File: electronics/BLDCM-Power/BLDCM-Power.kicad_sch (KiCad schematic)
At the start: 34 parts, among them J1 501920-3001, J2 53048-0310, J3 505578-0460, J4 505578-0460, J5 FTSH-107-01-L-DV-K, J6 12402012E212A, U1 INA239-Q1, U3 TMC6300-LA, U4 INA239-Q1, U5 TCAN1462, U6 INA239-Q1, U7 BAT54S

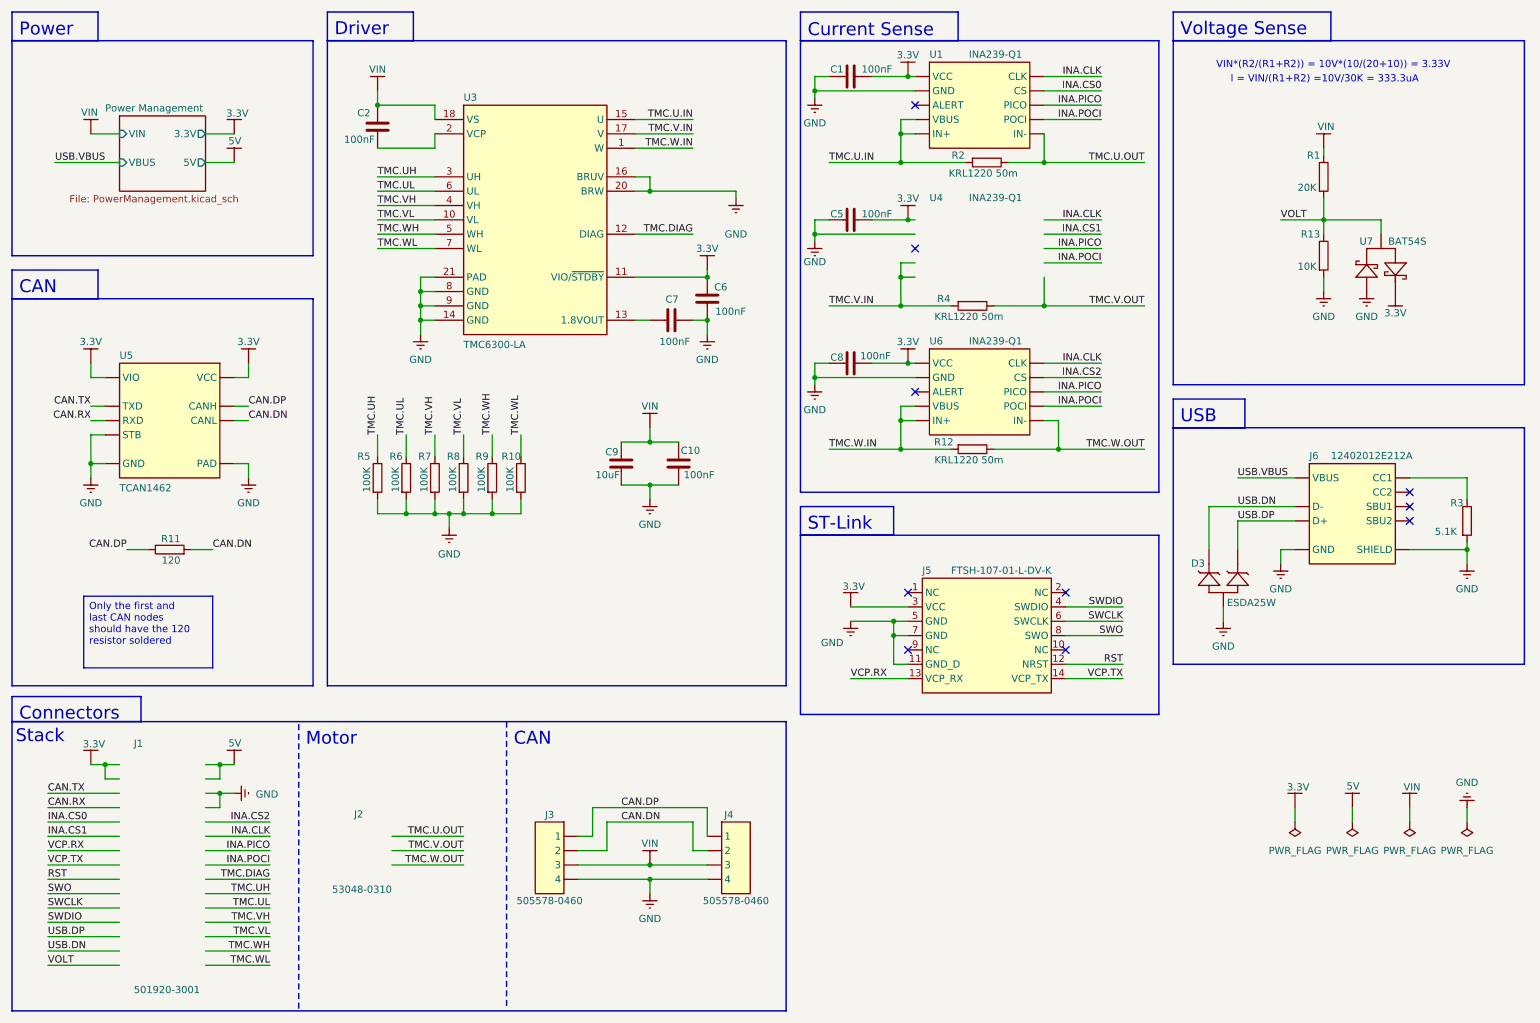
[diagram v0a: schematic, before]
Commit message: Feat(schematic): Replace INA239 with INA240
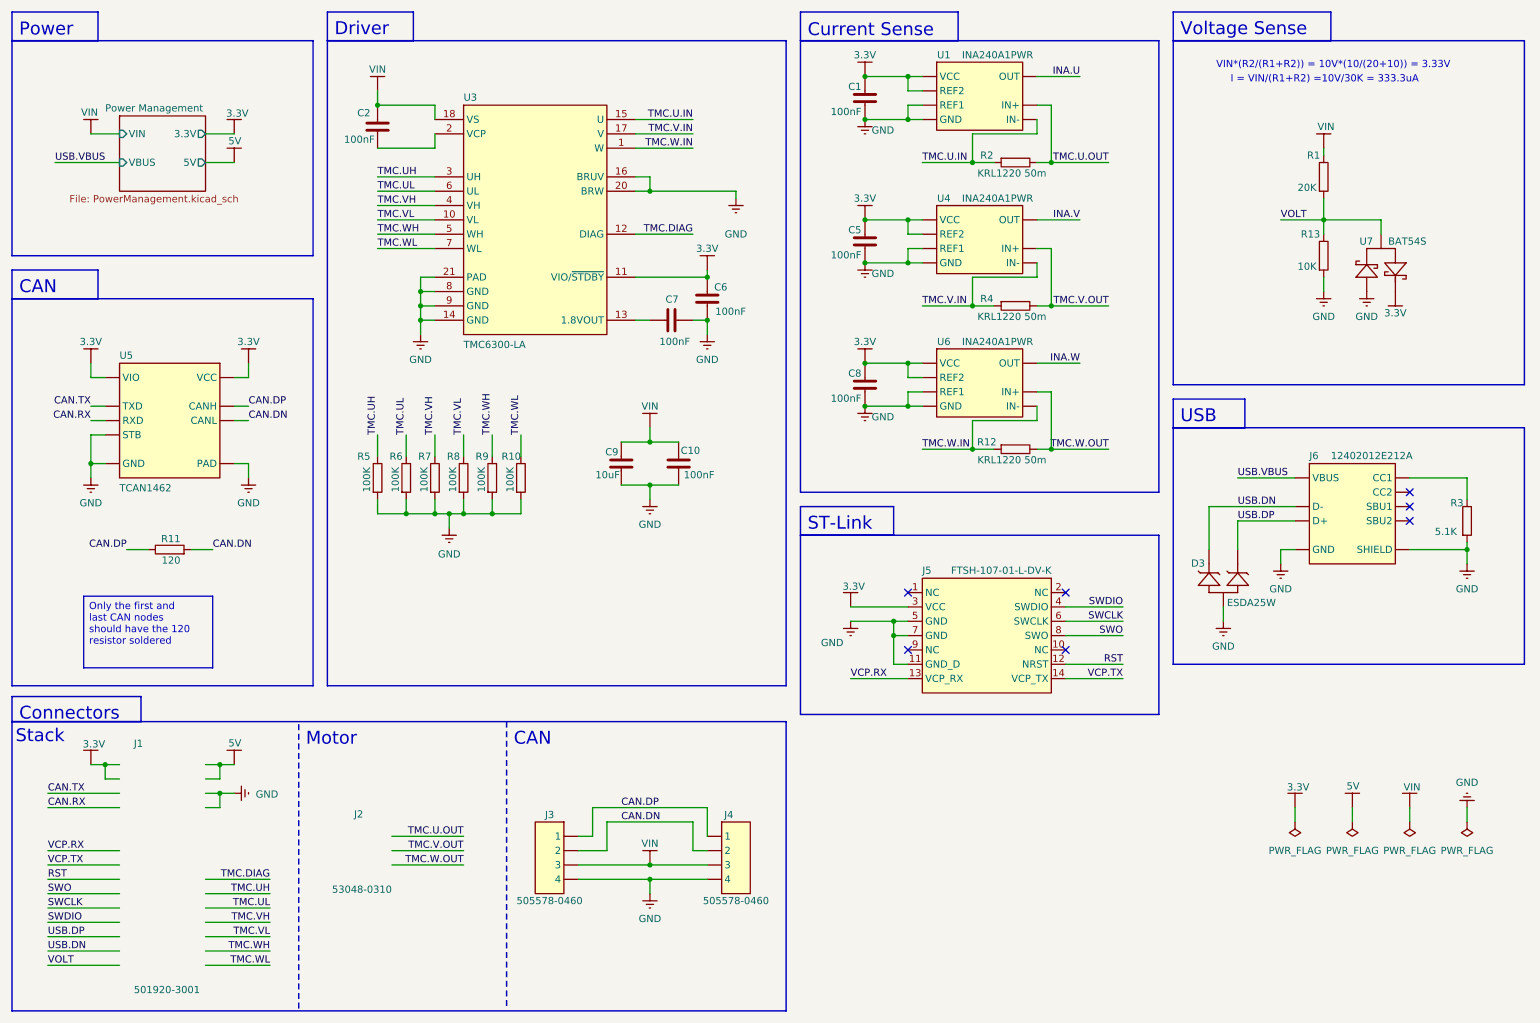
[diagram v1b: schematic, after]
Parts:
- removed U1, U4, U6: INA239-Q1, BrenoCQ:VSSOP-10, symbol BrenoCQ:INA239-Q1
- added U1, U4, U6: INA240A1PWR, BrenoCQ:TSSOP-8, symbol BrenoCQ:INA240AXPW
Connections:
- net 3.3V: now also U1.5 (VCC), U1.6 (REF2), U4.5 (VCC), U4.6 (REF2), U6.5 (VCC), U6.6 (REF2)
- net GND: now also U1.4 (GND), U1.7 (REF1), U4.4 (GND), U4.7 (REF1), U6.4 (GND), U6.7 (REF1)
- net TMC.U.IN: now also U1.3 (IN-)
- net TMC.U.OUT: now also U1.2 (IN+)
- net TMC.V.IN: now also U4.3 (IN-)
- net TMC.V.OUT: now also U4.2 (IN+)
- net TMC.W.IN: now also U6.3 (IN-)
- net TMC.W.OUT: now also U6.2 (IN+)
- new net INA.U: U1.8 (OUT)
- new net INA.V: U4.8 (OUT)
- new net INA.W: U6.8 (OUT)
- no-connect marks 10 -> 7
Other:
- moved on the sheet: C1, R2

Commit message: Feat(schematic): High frequency voltage sense
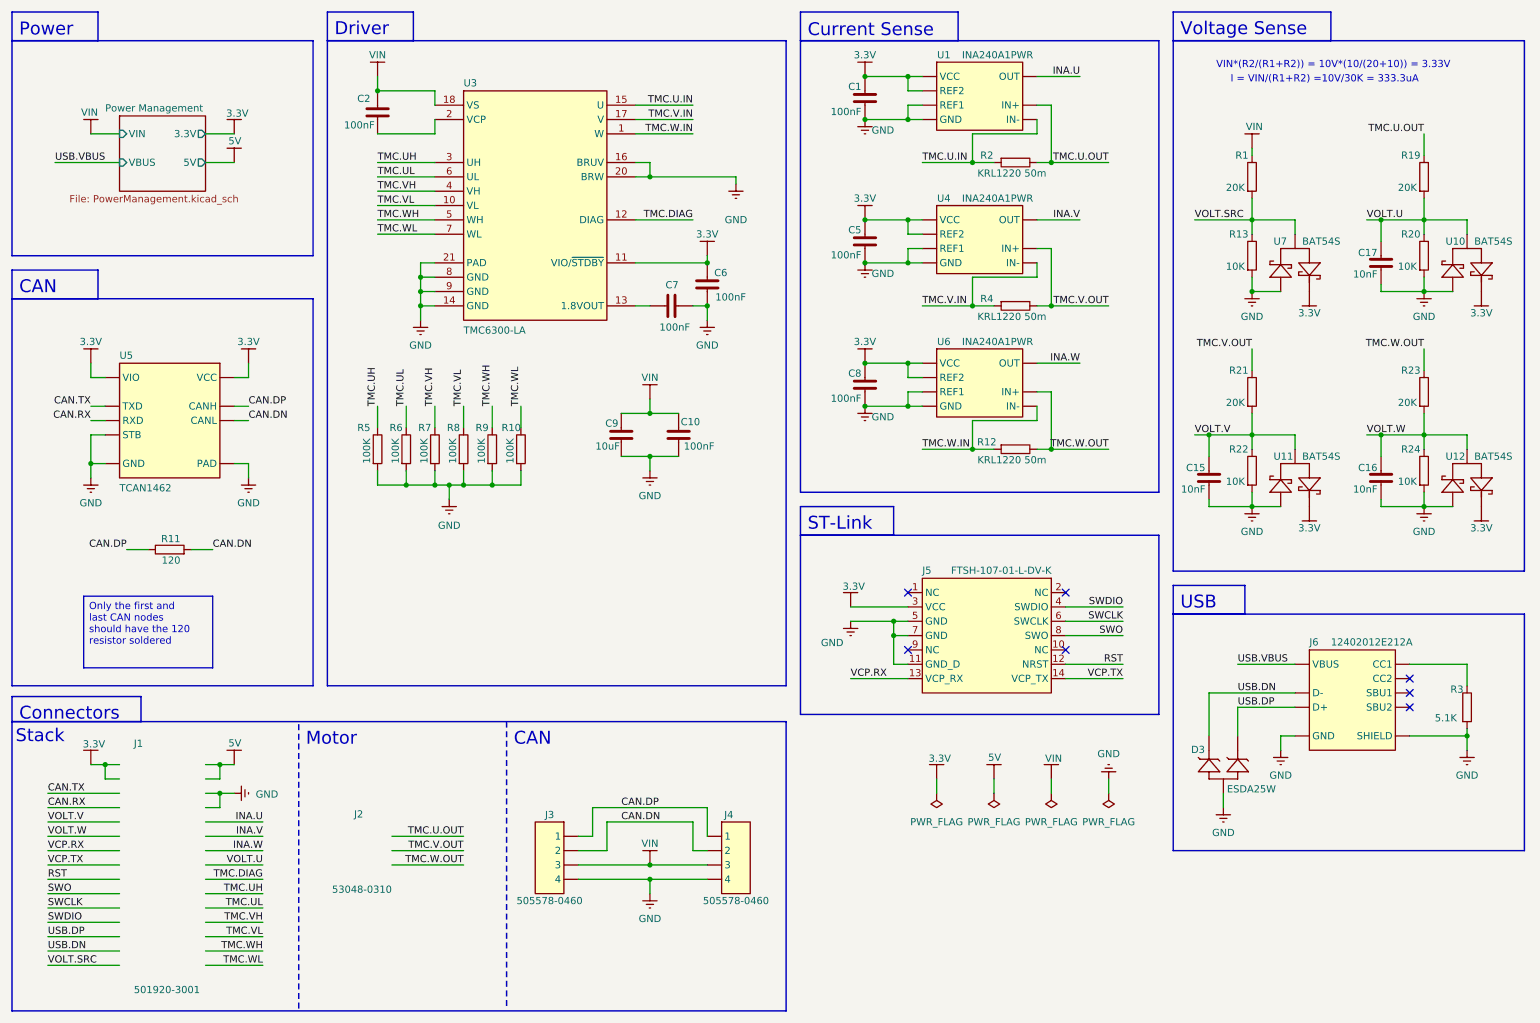
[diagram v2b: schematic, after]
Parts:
- added C15, C16, C17: 10nF, BrenoCQ:C_0402, symbol BrenoCQ:C
- added R19, R21, R23: 20K, BrenoCQ:R_0402, symbol BrenoCQ:R
- added R20, R22, R24: 10K, BrenoCQ:R_0402, symbol BrenoCQ:R
- added U10, U11, U12: BAT54S, BrenoCQ:SOT-23, symbol BrenoCQ:BAT54S
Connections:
- net 3.3V: now also U10.2, U11.2, U12.2
- net GND: now also C15.1, C16.1, C17.1, R20.1, R22.1, R24.1, U10.1, U11.1, U12.1
- net TMC.U.OUT: now also R19.2
- net TMC.V.OUT: now also R21.2
- net TMC.W.OUT: now also R23.2
- net VOLT renamed VOLT.SRC
- new net VOLT.U: C17.2, R19.1, R20.2, U10.3
- new net VOLT.V: C15.2, R21.1, R22.2, U11.3
- new net VOLT.W: C16.2, R23.1, R24.2, U12.3
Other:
- moved on the sheet: C10, C2, C6, C7, C9, D3, J6, R1, R10, R13, R3, R5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

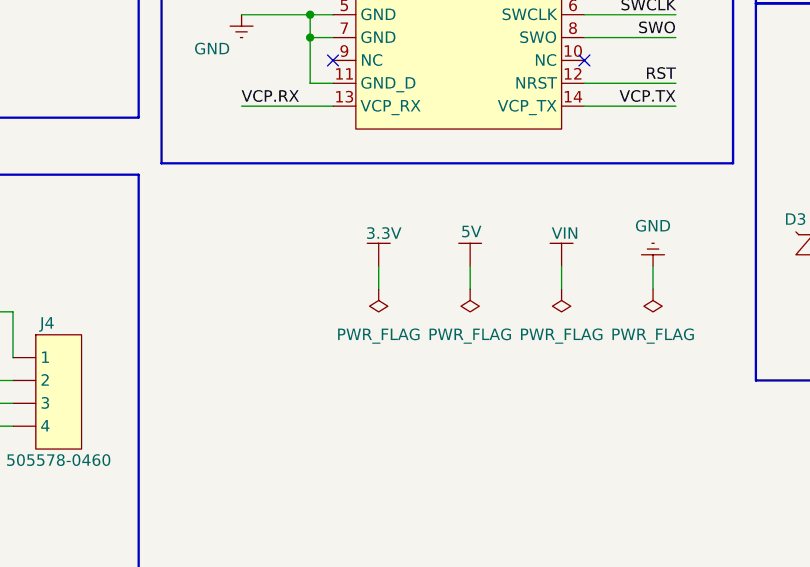
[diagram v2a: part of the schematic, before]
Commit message: Fix(schematic): Power board ERC errors
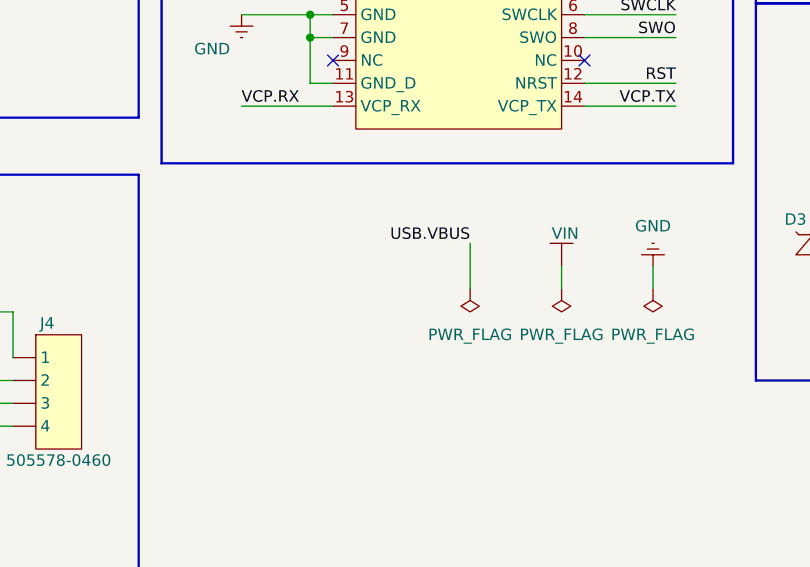
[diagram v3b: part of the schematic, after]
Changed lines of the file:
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@@
 	(wire
 		(pts
+			(xy 187.96 147.32) (xy 187.96 152.4)
+		)
+		(stroke
+			(width 0)
+			(type default)
+		)
+	)
+	(wire
+		(pts
 			(xy 48.26 182.88) (xy 58.42 182.88)
 		)
@@
 	(wire
 		(pts
-			(xy 177.8 149.86) (xy 177.8 152.4)
-		)
-		(stroke
-			(width 0)
-			(type default)
-		)
-	)
-	(wire
-		(pts
 			(xy 195.58 50.8) (xy 203.2 50.8)
 		)
@@
 	(wire
 		(pts
-			(xy 187.96 149.86) (xy 187.96 152.4)
-		)
-		(stroke
-			(width 0)
-			(type default)
-		)
-	)
-	(wire
-		(pts
 			(xy 233.68 38.1) (xy 233.68 39.37)
 		)
@@
 		)
 	)
+	(label "USB.VBUS"
+		(at 187.96 147.32 180)
+		(effects
+			(font
+				(size 1.27 1.27)
+			)
+			(justify right bottom)
+		)
+	)
 	(label "VCP.RX"
 		(at 162.56 132.08 0)
@@
 	)
 	(symbol
+		(lib_id "power:PWR_FLAG")
+		(at 187.96 152.4 180)
+		(unit 1)
+		(exclude_from_sim no)
+		(in_bom yes)
+		(on_board yes)
+		(dnp no)
+		(fields_autoplaced yes)
+		(property "Reference" "#FLG05"
+			(at 187.96 154.305 0)
+			(effects
+				(font
+					(size 1.27 1.27)
+				)
+				(hide yes)
+			)
+		)
+		(property "Value" "PWR_FLAG"
+			(at 187.96 157.48 0)
+			(effects
+				(font
+					(size 1.27 1.27)
+				)
+			)
+		)
+		(property "Footprint" ""
+			(at 187.96 152.4 0)
+			(effects
+				(font
+					(size 1.27 1.27)
+				)
+				(hide yes)
+			)
+		)
+		(property "Datasheet" "~"
+			(at 187.96 152.4 0)
+			(effects
+				(font
+					(size 1.27 1.27)
+				)
+				(hide yes)
+			)
+		)
+		(property "Description" "Special symbol for telling ERC where power comes from"
+			(at 187.96 152.4 0)
+			(effects
+				(font
+					(size 1.27 1.27)
+				)
+				(hide yes)
+			)
+		)
+		(pin "1"
+		)
+		(instances
+			(project "BLDCM-Power"
+				(path "/70c0b777-4ad9-403d-bed6-4daf67ef9f8e"
+					(reference "#FLG05")
+					(unit 1)
+				)
+			)
+		)
+	)
+	(symbol
 		(lib_id "BrenoCQ:R")
 		(at 99.06 91.44 90)
@@
 	)
 	(symbol
-		(lib_id "power:PWR_FLAG")
-		(at 177.8 152.4 180)
-		(unit 1)
-		(exclude_from_sim no)
-		(in_bom yes)
-		(on_board yes)
-		(dnp no)
-		(fields_autoplaced yes)
-		(property "Reference" "#FLG02"
-			(at 177.8 154.305 0)
-			(effects
-				(font
-					(size 1.27 1.27)
-				)
-				(hide yes)
-			)
-		)
-		(property "Value" "PWR_FLAG"
-			(at 177.8 157.48 0)
-			(effects
-				(font
-					(size 1.27 1.27)
-				)
-			)
-		)
-		(property "Footprint" ""
-			(at 177.8 152.4 0)
-			(effects
-				(font
-					(size 1.27 1.27)
-				)
-				(hide yes)
-			)
-		)
-		(property "Datasheet" "~"
-			(at 177.8 152.4 0)
-			(effects
-				(font
-					(size 1.27 1.27)
-				)
-				(hide yes)
-			)
-		)
-		(property "Description" "Special symbol for telling ERC where power comes from"
-			(at 177.8 152.4 0)
-			(effects
-				(font
-					(size 1.27 1.27)
-				)
-				(hide yes)
-			)
-		)
-		(pin "1"
-		)
-		(instances
-			(project "BLDCM-Power"
-				(path "/70c0b777-4ad9-403d-bed6-4daf67ef9f8e"
-					(reference "#FLG02")
-					(unit 1)
-				)
-			)
-		)
-	)
-	(symbol
 		(lib_id "BrenoCQ:GND")
 		(at 165.1 83.82 0)
@@
 	(symbol
 		(lib_id "BrenoCQ:VDD")
-		(at 187.96 149.86 0)
-		(unit 1)
-		(exclude_from_sim no)
-		(in_bom yes)
-		(on_board yes)
-		(dnp no)
-		(property "Reference" "#PWR06"
-			(at 187.96 149.86 0)
-			(effects
-				(font
-					(size 1.27 1.27)
-				)
-				(hide yes)
-			)
-		)
-		(property "Value" "5V"
-			(at 189.23 146.05 0)
-			(effects
-				(font
-					(size 1.27 1.27)
-				)
-				(justify right)
-			)
-		)
-		(property "Footprint" ""
-			(at 187.96 149.86 0)
-			(effects
-				(font
-					(size 1.27 1.27)
-				)
-				(hide yes)
-			)
-		)
-		(property "Datasheet" ""
-			(at 187.96 149.86 0)
-			(effects
-				(font
-					(size 1.27 1.27)
-				)
-				(hide yes)
-			)
-		)
-		(property "Description" "Source power symbol"
-			(at 187.96 153.67 0)
-			(effects
-				(font
-					(size 1.27 1.27)
-				)
-				(hide yes)
-			)
-		)
-		(pin "1"
-		)
-		(instances
-			(project "BLDCM-Power"
-				(path "/70c0b777-4ad9-403d-bed6-4daf67ef9f8e"
-					(reference "#PWR06")
-					(unit 1)
-				)
-			)
-		)
-	)
-	(symbol
-		(lib_id "BrenoCQ:VDD")
 		(at 165.1 76.2 0)
 		(unit 1)
@@
 	)
 	(symbol
-		(lib_id "BrenoCQ:VDD")
-		(at 177.8 149.86 0)
-		(unit 1)
-		(exclude_from_sim no)
-		(in_bom yes)
-		(on_board yes)
-		(dnp no)
-		(property "Reference" "#PWR0139"
-			(at 177.8 149.86 0)
-			(effects
-				(font
-					(size 1.27 1.27)
-				)
-				(hide yes)
-			)
-		)
-		(property "Value" "3.3V"
-			(at 180.34 146.2278 0)
-			(effects
-				(font
-					(size 1.27 1.27)
-				)
-				(justify right)
-			)
-		)
-		(property "Footprint" ""
-			(at 177.8 149.86 0)
-			(effects
-				(font
-					(size 1.27 1.27)
-				)
-				(hide yes)
-			)
-		)
-		(property "Datasheet" ""
-			(at 177.8 149.86 0)
-			(effects
-				(font
-					(size 1.27 1.27)
-				)
-				(hide yes)
-			)
-		)
-		(property "Description" "Source power symbol"
-			(at 177.8 153.67 0)
-			(effects
-				(font
-					(size 1.27 1.27)
-				)
-				(hide yes)
-			)
-		)
-		(pin "1"
-		)
-		(instances
-			(project "BLDCM-Power"
-				(path "/70c0b777-4ad9-403d-bed6-4daf67ef9f8e"
-					(reference "#PWR0139")
-					(unit 1)
-				)
-			)
-		)
-	)
-	(symbol
 		(lib_id "BrenoCQ:R")
 		(at 93.98 91.44 90)
@@
 					(unit 1)
 				)
-			)
-		)
-	)
-	(symbol
-		(lib_id "power:PWR_FLAG")
-		(at 187.96 152.4 180)
-		(unit 1)
-		(exclude_from_sim no)
-		(in_bom yes)
-		(on_board yes)
-		(dnp no)
-		(fields_autoplaced yes)
-		(property "Reference" "#FLG04"
-			(at 187.96 154.305 0)
-			(effects
-				(font
-					(size 1.27 1.27)
-				)
-				(hide yes)
-			)
-		)
-		(property "Value" "PWR_FLAG"
-			(at 187.96 157.48 0)
-			(effects
-				(font
-					(size 1.27 1.27)
-				)
-			)
-		)
-		(property "Footprint" ""
-			(at 187.96 152.4 0)
-			(effects
-				(font
-					(size 1.27 1.27)
-				)
-				(hide yes)
-			)
-		)
-		(property "Datasheet" "~"
-			(at 187.96 152.4 0)
-			(effects
-				(font
-					(size 1.27 1.27)
-				)
-				(hide yes)
-			)
-		)
-		(property "Description" "Special symbol for telling ERC where power comes from"
-			(at 187.96 152.4 0)
-			(effects
-				(font
-					(size 1.27 1.27)
-				)
-				(hide yes)
-			)
-		)
-		(pin "1"
-		)
-		(instances
-			(project "BLDCM-Power"
-				(path "/70c0b777-4ad9-403d-bed6-4daf67ef9f8e"
-					(reference "#FLG04")
-					(unit 1)
-				)

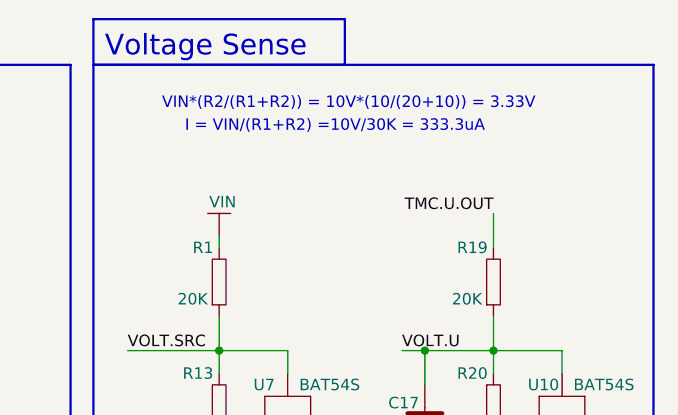
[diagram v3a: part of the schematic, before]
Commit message: Feat(pcb): Route phase voltage sense
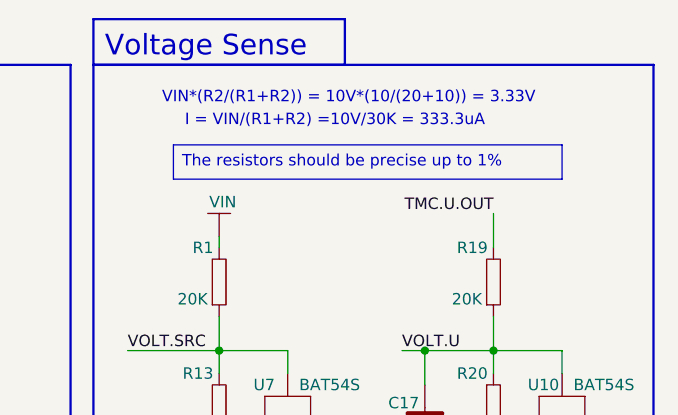
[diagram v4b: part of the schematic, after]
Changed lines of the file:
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@@
 	(text "I = VIN/(R1+R2) =10V/30K = 333.3uA"
 		(exclude_from_sim no)
-		(at 229.87 26.67 0)
+		(at 229.87 26.035 0)
 		(effects
 			(font
@@
 	(text "VIN*(R2/(R1+R2)) = 10V*(10/(20+10)) = 3.33V"
 		(exclude_from_sim no)
-		(at 227.33 24.13 0)
+		(at 227.33 23.495 0)
 		(effects
 			(font
@@
 		)
 	)
+	(text_box "The resistors should be precise up to 1%"
+		(exclude_from_sim no)
+		(at 228.6 27.94 0)
+		(size 43.18 3.81)
+		(margins 0.9525 0.9525 0.9525 0.9525)
+		(stroke
+			(width 0)
+			(type solid)
+			(color 0 0 0 1)
+		)
+		(fill
+			(type color)
+			(color 255 255 150 1)
+		)
+		(effects
+			(font
+				(size 1.27 1.27)
+			)
+			(justify left top)
+		)
+	)
